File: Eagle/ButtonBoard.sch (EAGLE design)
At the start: 8 parts

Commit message: - some modifications, corrections, ...
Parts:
- added LED1: Yellow, led:LED3MM
- added LED2: Red, led:LED3MM
- added R3: 470R, rcl:R-EU_0207/10
- added R4: 820R, rcl:R-EU_0207/10
- R1, R2: value (none) -> 470R
- X1: device con-molex:KK-156-8 -> con-molex:KK-156-10
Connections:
- new net N$11: LED2.A, R4.1
- new net N$12: LED1.A, R3.2
- new net N$13: R3.1, X1-2.S
- new net N$14: R4.2, X1-1.S
- net GND: now also LED1.C, LED2.C, X1-10.S; no longer X1-1.S
- net N$2: now also X1-3.S; no longer X1-8.S
- net N$3: now also X1-4.S; no longer X1-7.S
- net N$4: now also X1-9.S; no longer X1-2.S
- net N$6: now also X1-8.S; no longer X1-3.S
- net N$7: now also X1-7.S; no longer X1-4.S
- net N$8: now also X1-6.S; no longer X1-5.S
- net N$9: now also X1-5.S; no longer X1-6.S
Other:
- moved on the sheet: S1-1, S1-LED, S2, S3, S4, S5-1, S5-LED, X1-1, X1-2, X1-3, X1-4, X1-5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

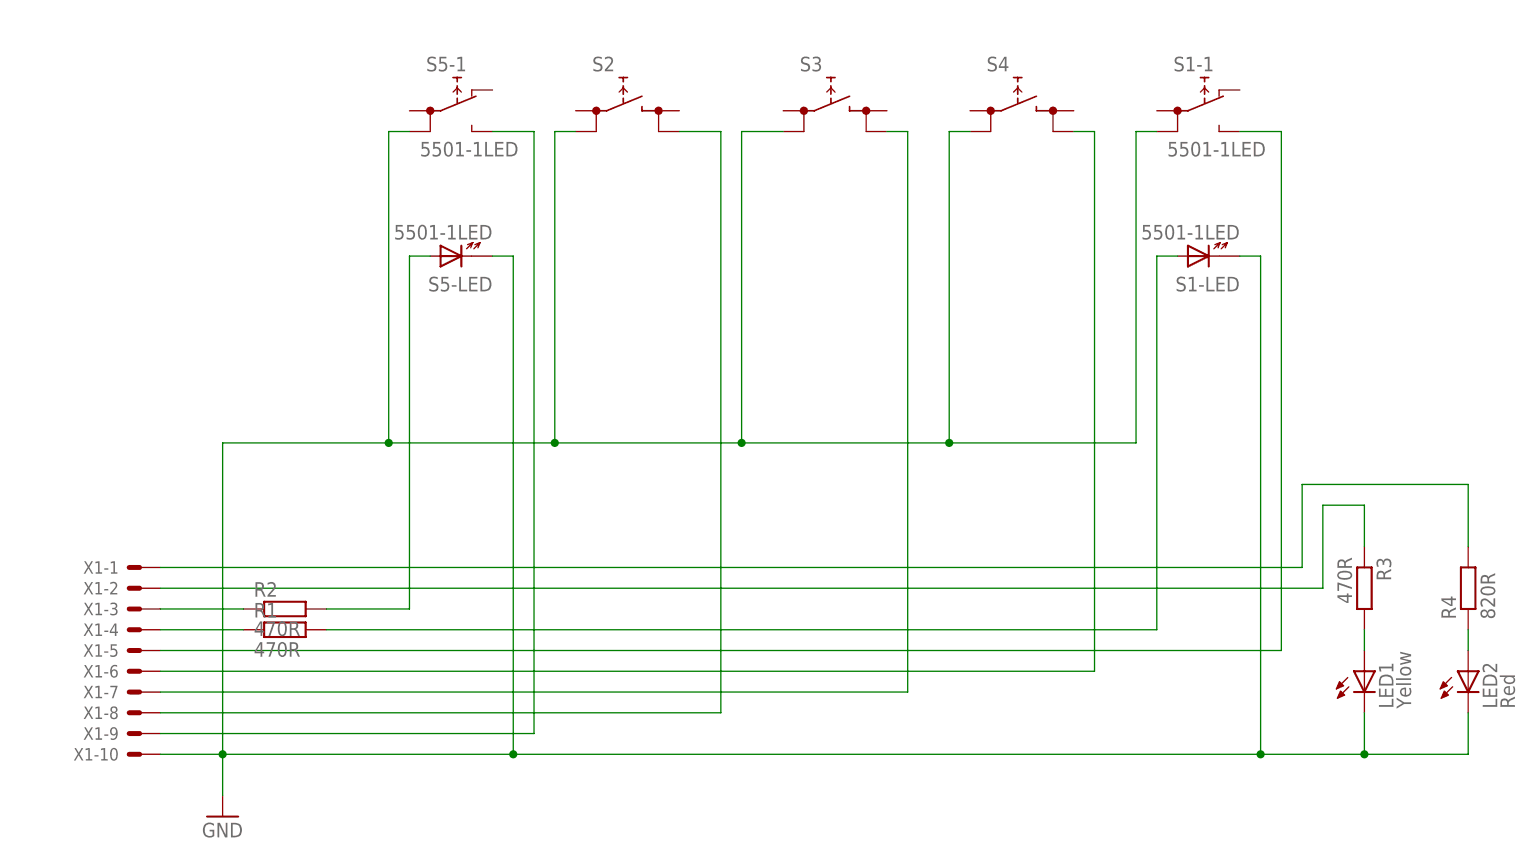
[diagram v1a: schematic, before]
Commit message: - corrections for RelayBoard1:   - using right connectors from library con-molex   - single sided routing - corrections for ButtonBoard:   - using right connector from library con-molex   - using right switches from library switch-misc (SRK/SRKL) - component placement & board layout for ButtonBoard done - CPUBoard:   - some components moved around the board   - re-routing (partially)
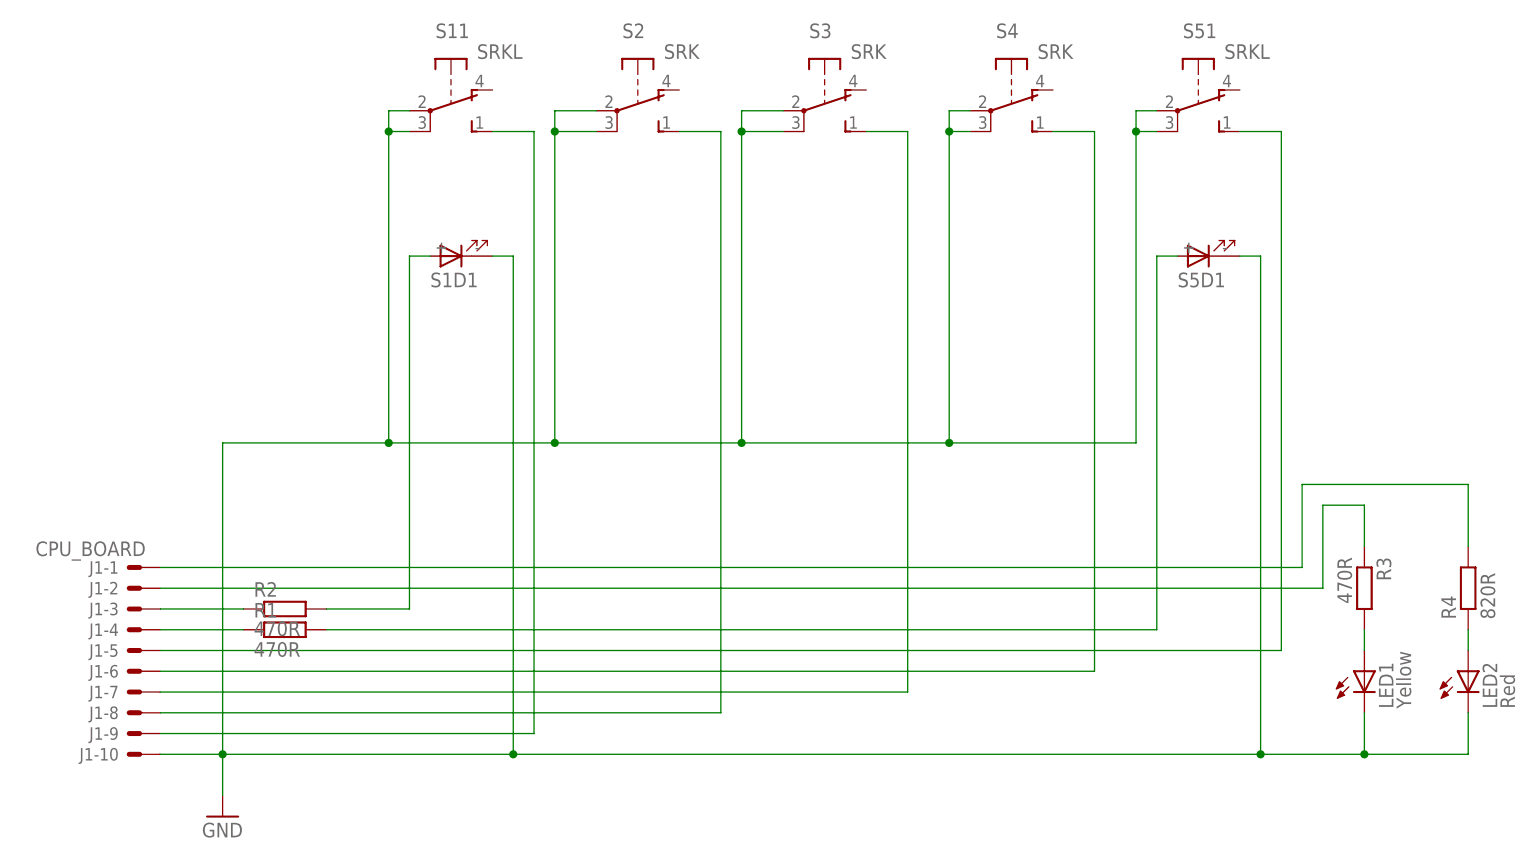
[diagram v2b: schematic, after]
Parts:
- removed X1: (no value), con-molex:KK-156-10
- added J1: CPU_BOARD, con-molex:22-05-7108-10
- S1, S5: value 5501-1LED -> SRKL; device switch:5501-1LED -> switch-misc:SRKL
- S2, S3, S4: value (none) -> SRK; device switch:REKN -> switch-misc:SRK
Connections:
- net GND: now also J1-10.S, S11.P, S11.P@1, S1D1.C, S2.P, S2.P@1, S3.P, S3.P@1, S4.P, S4.P@1, S51.P, S51.P@1, S5D1.C; no longer S1-1.1B, S1-LED.K, S2.0@B, S3.0@B, S4.0@B, S5-1.1B, S5-LED.K, X1-10.S
- net N$1: now also S1D1.A; no longer S5-LED.A
- net N$13: now also J1-2.S; no longer X1-2.S
- net N$14: now also J1-1.S; no longer X1-1.S
- net N$2: now also J1-3.S; no longer X1-3.S
- net N$3: now also J1-4.S; no longer X1-4.S
- net N$4: now also J1-9.S, S11.S; no longer S5-1.NO, X1-9.S
- net N$5: now also S5D1.A; no longer S1-LED.A
- net N$6: now also J1-8.S, S2.S; no longer S2.1@B, X1-8.S
- net N$7: now also J1-7.S, S3.S; no longer S3.1@B, X1-7.S
- net N$8: now also J1-6.S, S4.S; no longer S4.1@B, X1-6.S
- net N$9: now also J1-5.S, S51.S; no longer S1-1.NO, X1-5.S
